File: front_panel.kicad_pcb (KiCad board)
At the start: 4 copper layers, 0 parts

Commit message: Front and rear layout done
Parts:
- added REF**: MountingHole_3.5mm, MountingHole:MountingHole_3.5mm, F.Cu at (225.0, 128.3)
- added REF**: MountingHole_3.5mm, MountingHole:MountingHole_3.5mm, F.Cu at (69.4, 128.3)
- added REF**: MountingHole_3.5mm, MountingHole:MountingHole_3.5mm, F.Cu at (225.0, 105.8)
- added REF**: MountingHole_3.5mm, MountingHole:MountingHole_3.5mm, F.Cu at (69.4, 105.8)
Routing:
- net GND: vias 0 -> 115
- added copper zone on B.Cu, net GND
- added copper zone on F.Cu, net GND
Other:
- board outline added: 165.5 x 30.6 mm
- copper layers 4 -> 2
- board text added: "21V"
- board text added: "Error"
- board text added: "PCB must be 0.6mm thick"
- board text added: "Power"

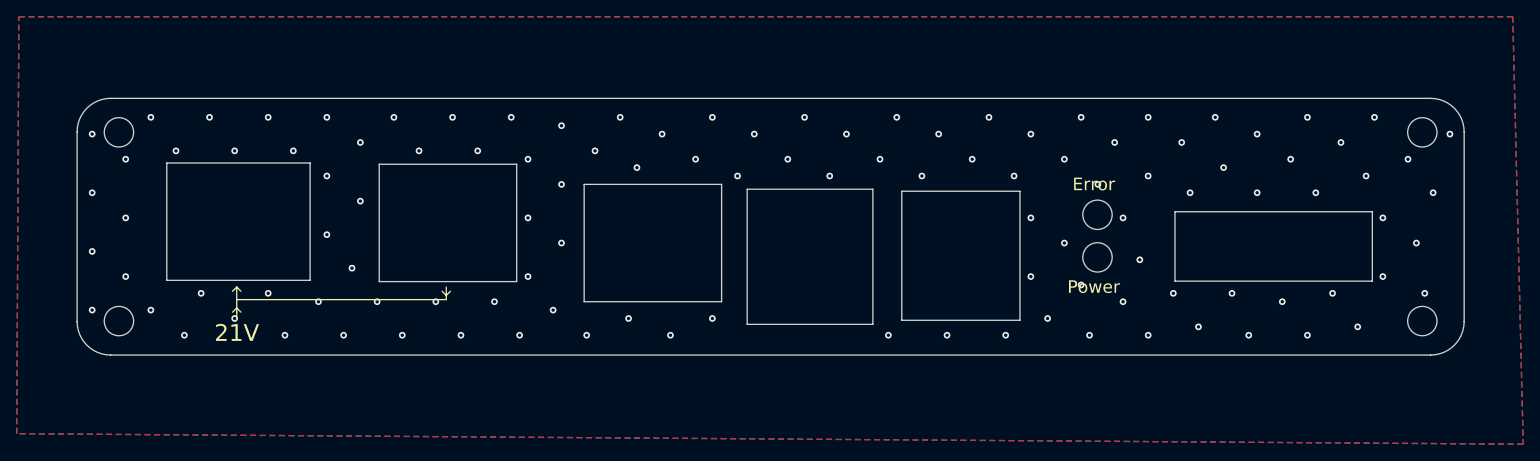
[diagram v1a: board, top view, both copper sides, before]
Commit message: Added KiBuzzard labels
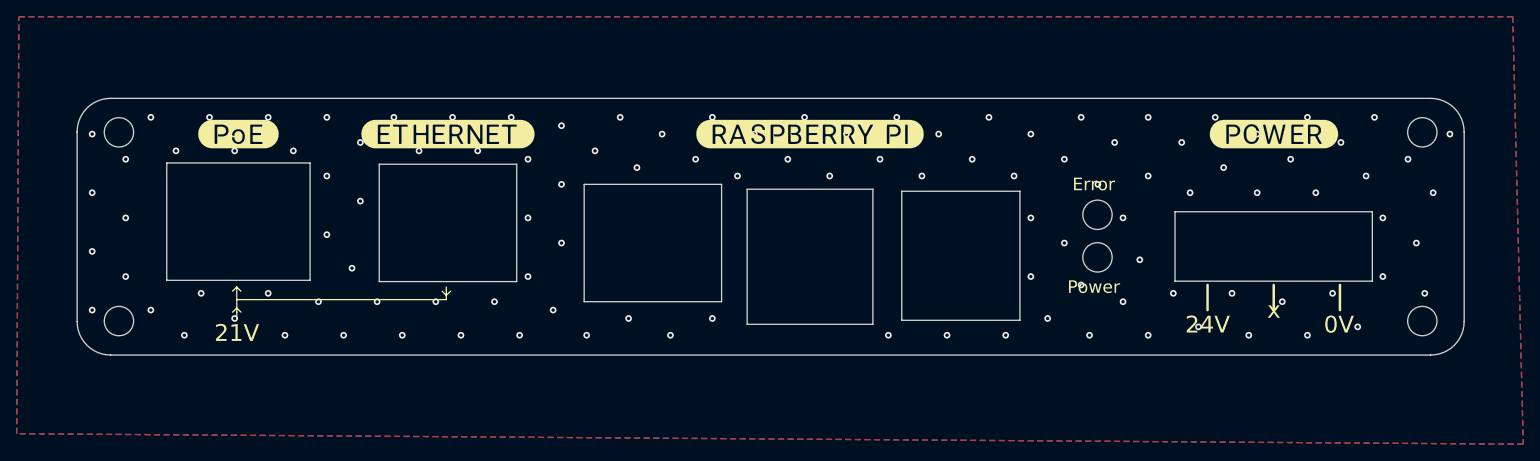
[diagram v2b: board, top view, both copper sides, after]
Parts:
- added ?: , buzzardLabel, F.Cu at (207.3, 106.0)
- added ?: , buzzardLabel, F.Cu at (151.9, 106.0)
- added ?: , buzzardLabel, F.Cu at (83.7, 106.0)
- added ?: , buzzardLabel, F.Cu at (108.7, 106.0)
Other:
- board text added: "0V"
- board text added: "24V"
- board text added: "x"
